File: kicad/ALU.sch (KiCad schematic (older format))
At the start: 1 part, among them U20 74LS245

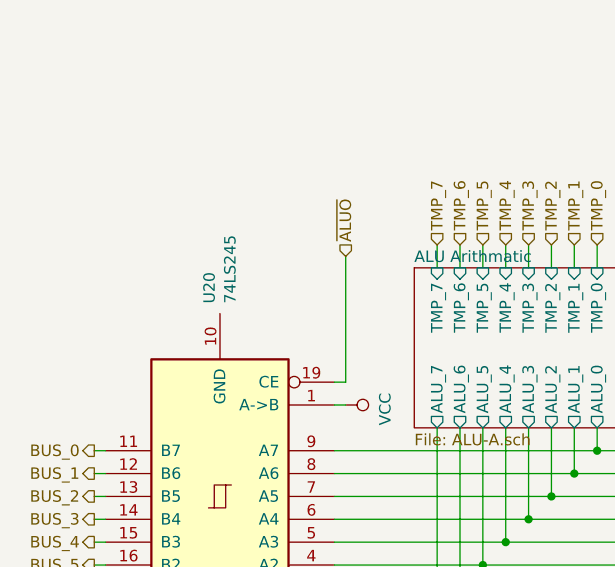
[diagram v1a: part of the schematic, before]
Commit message: Reorganize part references
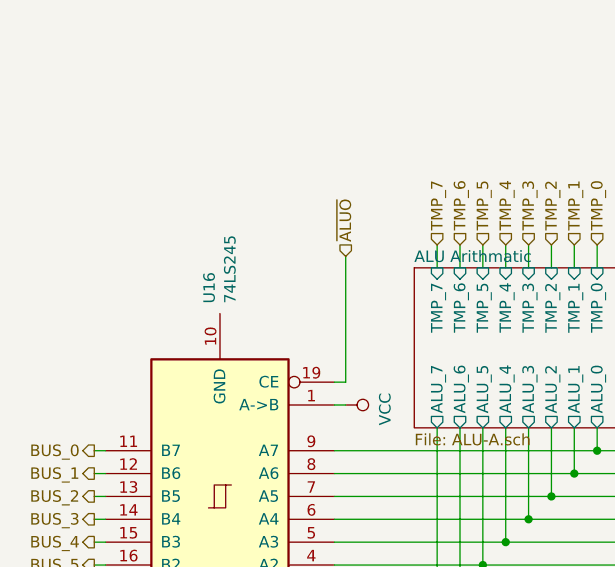
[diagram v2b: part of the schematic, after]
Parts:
- renumbered U20 to U16
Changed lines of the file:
@@
 $Descr USLetter 11000 8500
 encoding utf-8
-Sheet 19 26
+Sheet 6 26
 Title ""
 Date "2019-10-03"
@@
 A_0
 $Comp
-L 74xx:74LS245 U20
+L 74xx:74LS245 U16
 U 1 1 5F91404F
 P 1650 4150
-F 0 "U20" V 1696 3306 50  0000 R CNN
+F 0 "U16" V 1696 3306 50  0000 R CNN
 F 1 "74LS245" V 1605 3306 50  0000 R CNN
 F 2 "" H 1650 4150 50  0001 C CNN

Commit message: Up to v1.0 and plot
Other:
- note removed: "Instructions:\n - [X] ADD/ADC/ADI\n - [X] SUB/SBB/SUI\n - [ ] INR/INX\n - [ ] DCR/DCX\n - [ ] DAD\n - [X] ANA/ANI\n - [X] ORA/ORI\n - [X] XRA/XRI\n - [X] CMA\n - [X] CMP/CMI\n - [X] RRC/RLC/RAR/RAL\n - [ ] CMC\n - [ ] STC"
- moved on the sheet: U16
